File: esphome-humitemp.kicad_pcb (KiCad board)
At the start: 2 copper layers, 47.5 x 31.5 mm, 16 parts, among them J1 eflashy32, J2 USB_IN, J3 USB_OUT, U1 SHT35-DISB, U2 TLV75533PDBV, U3 ESP32-WROOM-32D

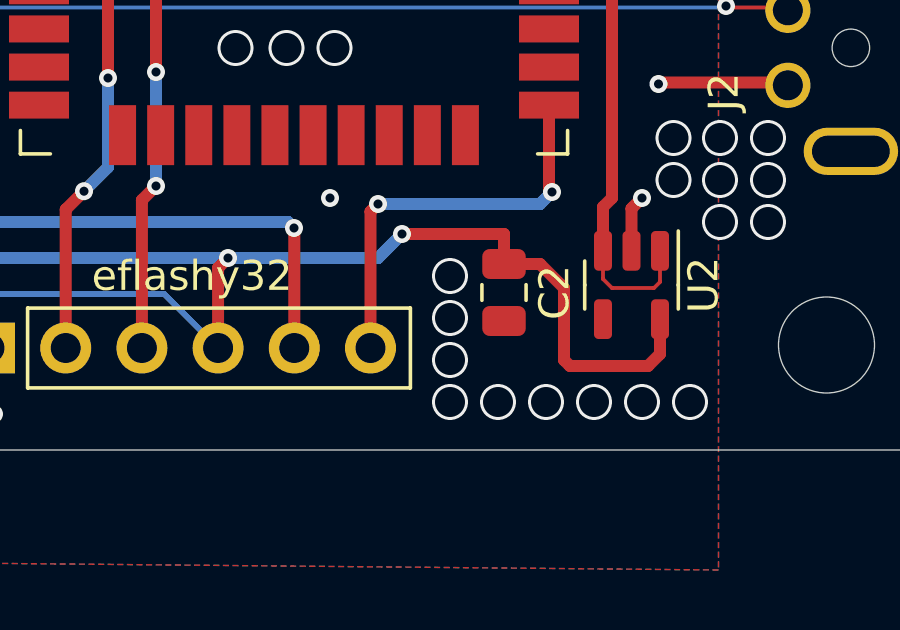
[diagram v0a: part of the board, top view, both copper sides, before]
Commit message: move thermal via slightly to avoid bad programmer placement
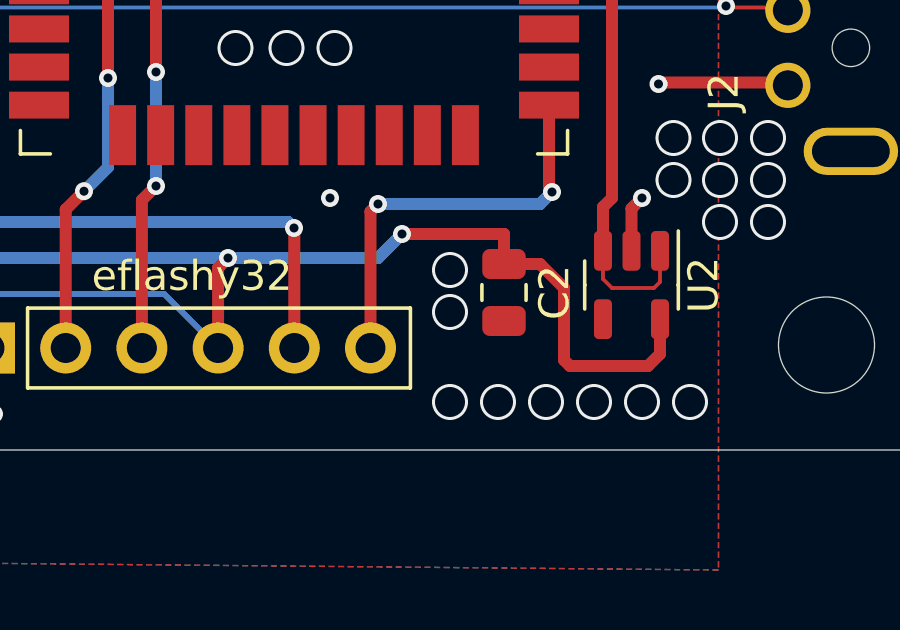
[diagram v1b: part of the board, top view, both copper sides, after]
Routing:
- net GND: vias 38 -> 37
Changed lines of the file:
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@@
   (via (at 131.2 72.4) (size 1.2) (drill 1) (layers "F.Cu" "B.Cu") (free) (net 2))
   (via (at 104.4 73.8) (size 1.2) (drill 1) (layers "F.Cu" "B.Cu") (free) (net 2))
-  (via (at 122.2 74.2) (size 1.2) (drill 1) (layers "F.Cu" "B.Cu") (free) (net 2))
+  (via (at 122.2 74) (size 1.2) (drill 1) (layers "F.Cu" "B.Cu") (free) (net 2))
   (via (at 99.6 73.2) (size 1.2) (drill 1) (layers "F.Cu" "B.Cu") (free) (net 2))
   (via (at 128.6 78.4) (size 1.2) (drill 1) (layers "F.Cu" "B.Cu") (free) (net 2))
@@
   (via (at 98.4 78.4) (size 1.2) (drill 1) (layers "F.Cu" "B.Cu") (free) (net 2))
   (via (at 116.75 66.6) (size 1.2) (drill 1) (layers "F.Cu" "B.Cu") (free) (net 2))
-  (via (at 122.2 77) (size 1.2) (drill 1) (layers "F.Cu" "B.Cu") (free) (net 2))
   (via (at 128.6 71.6) (size 0.6) (drill 0.3) (layers "F.Cu" "B.Cu") (net 2))
   (via (at 118.35 66.6) (size 1.2) (drill 1) (layers "F.Cu" "B.Cu") (free) (net 2))
   (via (at 107 78.8) (size 0.6) (drill 0.3) (layers "F.Cu" "B.Cu") (net 2))
   (via (at 131.2 71) (size 1.2) (drill 1) (layers "F.Cu" "B.Cu") (free) (net 2))
-  (via (at 122.2 75.6) (size 1.2) (drill 1) (layers "F.Cu" "B.Cu") (free) (net 2))
+  (via (at 122.2 75.4) (size 1.2) (drill 1) (layers "F.Cu" "B.Cu") (free) (net 2))
   (via (at 127 78.4) (size 1.2) (drill 1) (layers "F.Cu" "B.Cu") (free) (net 2))
   (via (at 123.8 78.4) (size 1.2) (drill 1) (layers "F.Cu" "B.Cu") (free) (net 2))

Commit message: v2 ecad
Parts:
- removed C3: 10uF, Capacitor_SMD:C_0805_2012Metric
- removed H3: MountingHole, MountingHole:MountingHole_3.2mm_M3
- removed J1: eflashy32, Connector_PinHeader_2.54mm:PinHeader_1x06_P2.54mm_Vertical
- removed J3: USB_OUT, Connector_USB:USB_A_Molex_67643_Horizontal
- removed R1: 10k, Resistor_SMD:R_0805_2012Metric
- removed U2: TLV75533PDBV, Package_TO_SOT_SMD:SOT-23-5
- added C4: 10u, Capacitor_SMD:C_0805_2012Metric, F.Cu at (117.8, 65.8)
- added C5: 0.1u, Capacitor_SMD:C_0603_1608Metric, F.Cu at (98.2, 69.5)
- added C6: 10u, Capacitor_SMD:C_0805_2012Metric, F.Cu at (97.9, 67.5)
- added R4: 10k, Resistor_SMD:R_0402_1005Metric, F.Cu at (121.0, 64.8)
- added R5: 10k, Resistor_SMD:R_0402_1005Metric, F.Cu at (121.0, 66.8)
- added R6: 10k, Resistor_SMD:R_0402_1005Metric, F.Cu at (121.0, 63.8)
- added SW1: RESET, Button_Switch_SMD:SW_Push_1P1T_XKB_TS-1187A, F.Cu at (122.0, 74.0)
- added U4: ESP32-C3-MINI-1, Espressif:ESP32-C3-MINI-1, F.Cu at (98.6, 59.0)
- R2, R3: footprint Resistor_SMD:R_0805_2012Metric -> Resistor_SMD:R_0402_1005Metric
- U1: value SHT35-DISB -> SHT3x
- U3: value ESP32-WROOM-32D -> AMS1117-3.3; footprint RF_Module:ESP32-WROOM-32 -> Package_TO_SOT_SMD:SOT-223-3_TabPin2
- moved C2 22.2 mm to (116.0, 54.0)
- moved H4 17.2 mm to (100.0, 36.0)
- moved R3 11.6 mm to (121.0, 62.8), turned to 180 degrees
- moved R2 11.1 mm to (121.0, 65.8), turned to 180 degrees
- moved U1 8.00 mm to (93.0, 77.0), turned to -90 degrees
- moved U3 6.66 mm to (122.0, 55.9), turned to 90 degrees
- moved C1 5.34 mm to (124.0, 64.0)
- moved H1 4.04 mm to (131.0, 54.0)
- moved H2 3.78 mm to (131.0, 76.0)
- moved J2 3.41 mm to (132.2, 65.0)
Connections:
- J2 pad 2: Net-(J2-Pad2) -> D-
- J2 pad 3: Net-(J2-Pad3) -> D+
- U1 pad 3: (no net) -> unconnected-(U1-ALERT-Pad3)
- U1 pad 6: (no net) -> unconnected-(U1-~{RESET}-Pad6)
- U3 pad 3: /EN -> VBUS
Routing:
- net GND: track 40.8 -> 90.4 mm, vias 37 -> 25
- net VBUS: track 50.3 -> 11.0 mm, vias 1 -> 0
- net D+: track 0.00 -> 39.2 mm, vias 0 -> 1
- net D-: track 0.00 -> 39.2 mm, vias 0 -> 1
- net /TXD: track 35.0 -> 0.00 mm, vias 4 -> 0
- net +3V3: track 108.7 -> 74.4 mm, vias 6 -> 4
- net Net-(J2-Pad3): track 33.4 -> 0.00 mm, vias 1 -> 0
- net Net-(J2-Pad2): track 33.4 -> 0.00 mm, vias 1 -> 0
- net /RXD: track 32.4 -> 0.00 mm, vias 4 -> 0
- net Net-(U4-GPIO2/ADC1_CH2): track 0.00 -> 22.4 mm, vias 0 -> 2
- net Net-(U4-GPIO8): track 0.00 -> 22.3 mm, vias 0 -> 2
- net /GPIO0: track 13.8 -> 35.0 mm, vias 2 -> 0
- net /EN: track 40.7 -> 19.8 mm, vias 4 -> 2
- net SDA: track 44.9 -> 38.1 mm, vias 4 -> 2
- net SCL: track 47.3 -> 48.1 mm, vias 2 -> 6
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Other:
- board size 47.5 x 31.5 mm -> 45 x 30 mm
- board text added: "<<hash>>"
- board text added: "esphome-humitemp v2"
- board text removed: "esphome-humitemp v1"
